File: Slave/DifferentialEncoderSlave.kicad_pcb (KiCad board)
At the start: 4 copper layers, 20 x 29 mm, 17 parts, among them J1 RJ45_Shielded, U1 SN75C1167, U2 MA730, U3 LDFM33PVR

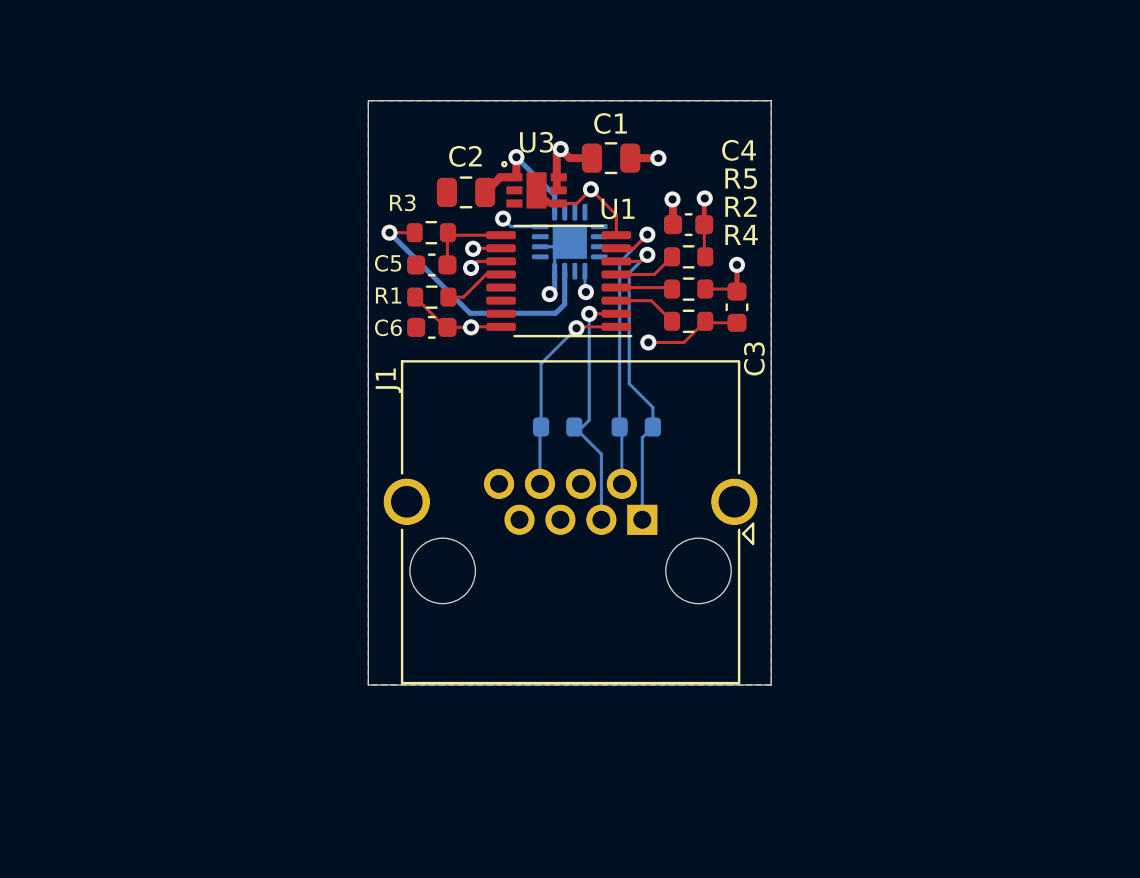
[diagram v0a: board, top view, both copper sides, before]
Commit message: Update board outline
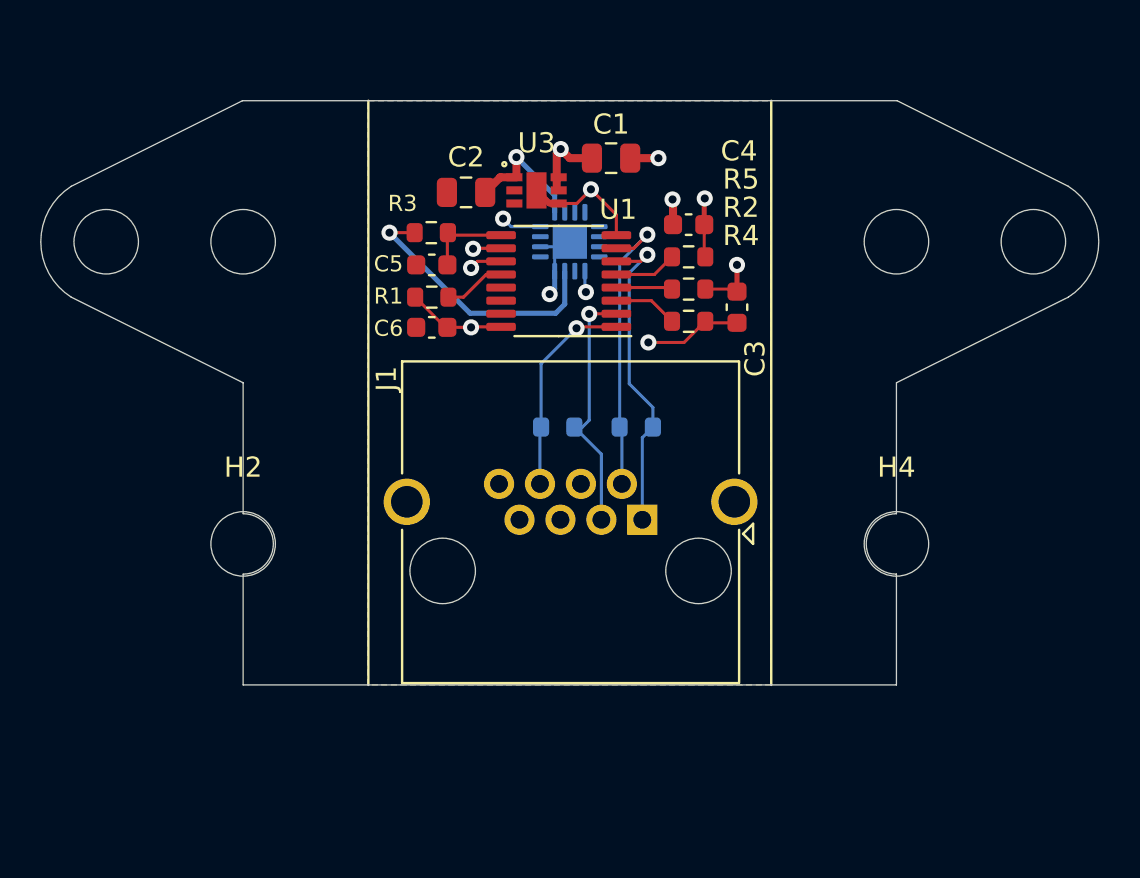
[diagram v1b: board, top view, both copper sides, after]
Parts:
- added H1: MountingHole, MountingHole:MountingHole_3.2mm_M3_DIN965, F.Cu at (138.2, 68.0)
- added H2: MountingHole, MountingHole:MountingHole_3.2mm_M3_DIN965, F.Cu at (105.8, 83.0)
- added H3: MountingHole, MountingHole:MountingHole_3.2mm_M3_DIN965, F.Cu at (105.8, 68.0)
- added H4: MountingHole, MountingHole:MountingHole_3.2mm_M3_DIN965, F.Cu at (138.2, 83.0)
- added H5: MountingHole, MountingHole:MountingHole_3.2mm_M3_DIN965, F.Cu at (99.0, 68.0)
- added H6: MountingHole, MountingHole:MountingHole_3.2mm_M3_DIN965, F.Cu at (145.0, 68.0)
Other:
- board size 20 x 29 mm -> 52.5 x 29 mm

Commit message: Use 3mm holes
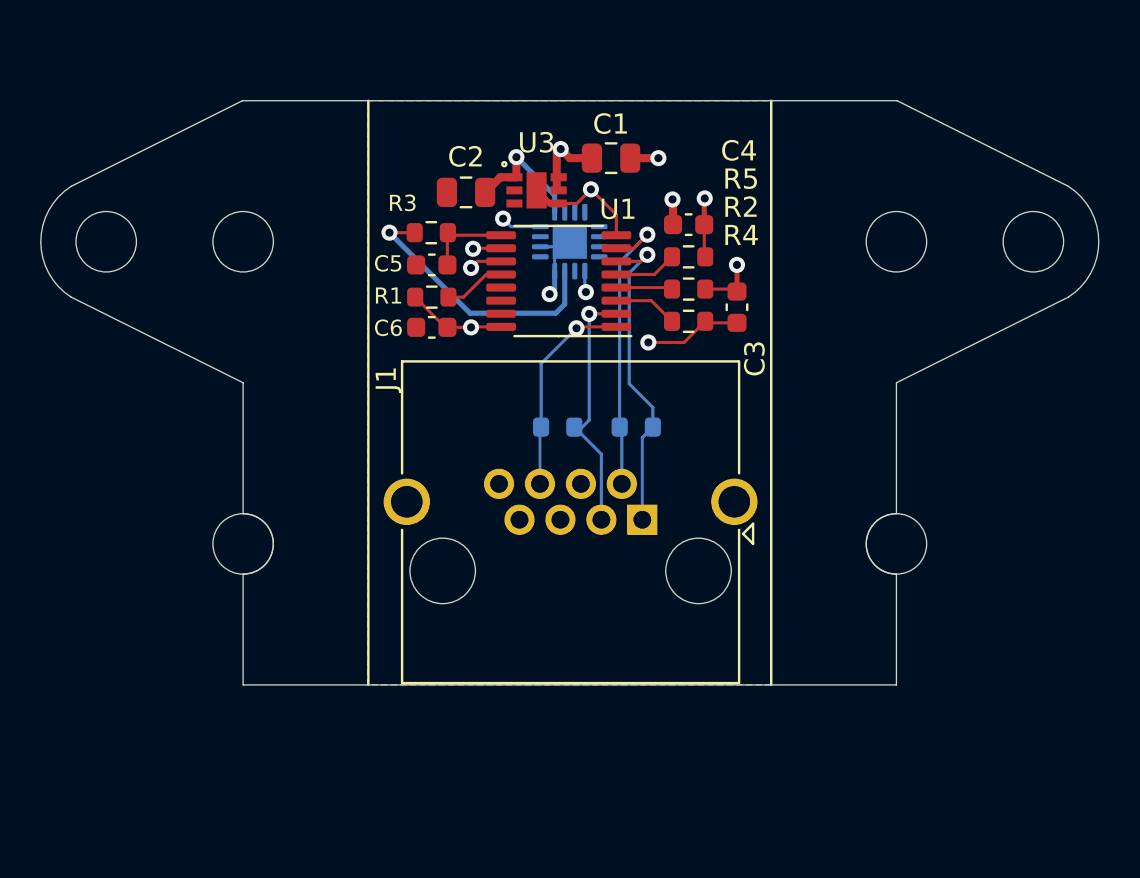
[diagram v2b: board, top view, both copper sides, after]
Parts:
- H1, H2, H3, H4, H5, H6: footprint MountingHole:MountingHole_3.2mm_M3_DIN965 -> MountingHole:MountingHole_3mm
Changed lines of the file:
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@@
     (add_net "Net-(U3-Pad3)")
   )
-  (module MountingHole:MountingHole_3.2mm_M3_DIN965 (layer F.Cu)
+  (module MountingHole:MountingHole_3mm (layer F.Cu)
     (at 138.215 83)
-    (descr "Mounting Hole 3.2mm, no annular, M3, DIN965")
-    (tags "mounting hole 3.2mm no annular m3 din965")
+    (descr "Mounting Hole 3mm, no annular")
+    (tags "mounting hole 3mm no annular")
     (attr virtual)
-    (fp_text reference H4 (at 0 -3.8) (layer F.SilkS)
+    (fp_text reference H4 (at -2.215 -4) (layer F.SilkS) hide
       (effects (font (size 1 1) (thickness 0.15)))
     )
-    (fp_text value MountingHole (at 0 3.8) (layer F.Fab)
+    (fp_text value MountingHole (at 0 4) (layer F.Fab)
       (effects (font (size 1 1) (thickness 0.15)))
     )
@@
       (effects (font (size 1 1) (thickness 0.15)))
     )
-    (fp_circle (center 0 0) (end 2.8 0) (layer Cmts.User) (width 0.15))
-    (fp_circle (center 0 0) (end 3.05 0) (layer F.CrtYd) (width 0.05))
-    (pad 1 np_thru_hole circle (at 0 0) (size 3.2 3.2) (drill 3.2) (layers *.Cu *.Mask))
+    (fp_circle (center 0 0) (end 3 0) (layer Cmts.User) (width 0.15))
+    (fp_circle (center 0 0) (end 3.25 0) (layer F.CrtYd) (width 0.05))
+    (pad 1 np_thru_hole circle (at 0 0) (size 3 3) (drill 3) (layers *.Cu *.Mask))
   )
-  (module MountingHole:MountingHole_3.2mm_M3_DIN965 (layer F.Cu)
+  (module MountingHole:MountingHole_3mm (layer F.Cu)
     (at 105.785 83)
-    (descr "Mounting Hole 3.2mm, no annular, M3, DIN965")
-    (tags "mounting hole 3.2mm no annular m3 din965")
+    (descr "Mounting Hole 3mm, no annular")
+    (tags "mounting hole 3mm no annular")
     (attr virtual)
-    (fp_text reference H2 (at 0 -3.8) (layer F.SilkS)
+    (fp_text reference H2 (at 2.215 -3.75) (layer F.SilkS) hide
       (effects (font (size 1 1) (thickness 0.15)))
     )
-    (fp_text value MountingHole (at 0 3.8) (layer F.Fab)
+    (fp_text value MountingHole (at 0 4) (layer F.Fab)
       (effects (font (size 1 1) (thickness 0.15)))
     )
@@
       (effects (font (size 1 1) (thickness 0.15)))
     )
-    (fp_circle (center 0 0) (end 2.8 0) (layer Cmts.User) (width 0.15))
-    (fp_circle (center 0 0) (end 3.05 0) (layer F.CrtYd) (width 0.05))
-    (pad 1 np_thru_hole circle (at 0 0) (size 3.2 3.2) (drill 3.2) (layers *.Cu *.Mask))
+    (fp_circle (center 0 0) (end 3 0) (layer Cmts.User) (width 0.15))
+    (fp_circle (center 0 0) (end 3.25 0) (layer F.CrtYd) (width 0.05))
+    (pad 1 np_thru_hole circle (at 0 0) (size 3 3) (drill 3) (layers *.Cu *.Mask))
   )
-  (module MountingHole:MountingHole_3.2mm_M3_DIN965 (layer F.Cu)
+  (module MountingHole:MountingHole_3mm (layer F.Cu)
     (at 145.0125 68)
-    (descr "Mounting Hole 3.2mm, no annular, M3, DIN965")
-    (tags "mounting hole 3.2mm no annular m3 din965")
+    (descr "Mounting Hole 3mm, no annular")
+    (tags "mounting hole 3mm no annular")
     (attr virtual)
-    (fp_text reference H6 (at 0 -3.8) (layer F.SilkS) hide
+    (fp_text reference H6 (at -3.0125 -3.5) (layer F.SilkS) hide
       (effects (font (size 1 1) (thickness 0.15)))
     )
-    (fp_text value MountingHole (at 0 3.8) (layer F.Fab)
+    (fp_text value MountingHole (at 0 4) (layer F.Fab)
       (effects (font (size 1 1) (thickness 0.15)))
     )
@@
       (effects (font (size 1 1) (thickness 0.15)))
     )
-    (fp_circle (center 0 0) (end 2.8 0) (layer Cmts.User) (width 0.15))
-    (fp_circle (center 0 0) (end 3.05 0) (layer F.CrtYd) (width 0.05))
-    (pad 1 np_thru_hole circle (at 0 0) (size 3.2 3.2) (drill 3.2) (layers *.Cu *.Mask))
+    (fp_circle (center 0 0) (end 3 0) (layer Cmts.User) (width 0.15))
+    (fp_circle (center 0 0) (end 3.25 0) (layer F.CrtYd) (width 0.05))
+    (pad 1 np_thru_hole circle (at 0 0) (size 3 3) (drill 3) (layers *.Cu *.Mask))
   )
-  (module MountingHole:MountingHole_3.2mm_M3_DIN965 (layer F.Cu)
+  (module MountingHole:MountingHole_3mm (layer F.Cu)
     (at 98.9875 68)
-    (descr "Mounting Hole 3.2mm, no annular, M3, DIN965")
-    (tags "mounting hole 3.2mm no annular m3 din965")
+    (descr "Mounting Hole 3mm, no annular")
+    (tags "mounting hole 3mm no annular")
     (attr virtual)
-    (fp_text reference H5 (at 0 -3.8) (layer F.SilkS) hide
+    (fp_text reference H5 (at 3.5125 -3.5) (layer F.SilkS) hide
       (effects (font (size 1 1) (thickness 0.15)))
     )
-    (fp_text value MountingHole (at 0 3.8) (layer F.Fab)
+    (fp_text value MountingHole (at 0 4) (layer F.Fab)
       (effects (font (size 1 1) (thickness 0.15)))
     )
@@
       (effects (font (size 1 1) (thickness 0.15)))
     )
-    (fp_circle (center 0 0) (end 2.8 0) (layer Cmts.User) (width 0.15))
-    (fp_circle (center 0 0) (end 3.05 0) (layer F.CrtYd) (width 0.05))
-    (pad 1 np_thru_hole circle (at 0 0) (size 3.2 3.2) (drill 3.2) (layers *.Cu *.Mask))
+    (fp_circle (center 0 0) (end 3 0) (layer Cmts.User) (width 0.15))
+    (fp_circle (center 0 0) (end 3.25 0) (layer F.CrtYd) (width 0.05))
+    (pad 1 np_thru_hole circle (at 0 0) (size 3 3) (drill 3) (layers *.Cu *.Mask))
   )
-  (module MountingHole:MountingHole_3.2mm_M3_DIN965 (layer F.Cu)
-    (at 138.215 68)
-    (descr "Mounting Hole 3.2mm, no annular, M3, DIN965")
-    (tags "mounting hole 3.2mm no annular m3 din965")
+  (module MountingHole:MountingHole_3mm (layer F.Cu)
+    (at 105.785 68)
+    (descr "Mounting Hole 3mm, no annular")
+    (tags "mounting hole 3mm no annular")
     (attr virtual)
-    (fp_text reference H1 (at -3.965 -3.25) (layer F.SilkS) hide
+    (fp_text reference H3 (at 0 -4) (layer F.SilkS) hide
       (effects (font (size 1 1) (thickness 0.15)))
     )
-    (fp_text value MountingHole (at 0 3.8) (layer F.Fab)
+    (fp_text value MountingHole (at 0 4) (layer F.Fab)
       (effects (font (size 1 1) (thickness 0.15)))
     )
@@
       (effects (font (size 1 1) (thickness 0.15)))
     )
-    (fp_circle (center 0 0) (end 2.8 0) (layer Cmts.User) (width 0.15))
-    (fp_circle (center 0 0) (end 3.05 0) (layer F.CrtYd) (width 0.05))
-    (pad 1 np_thru_hole circle (at 0 0) (size 3.2 3.2) (drill 3.2) (layers *.Cu *.Mask))
+    (fp_circle (center 0 0) (end 3 0) (layer Cmts.User) (width 0.15))
+    (fp_circle (center 0 0) (end 3.25 0) (layer F.CrtYd) (width 0.05))
+    (pad 1 np_thru_hole circle (at 0 0) (size 3 3) (drill 3) (layers *.Cu *.Mask))
   )
-  (module MountingHole:MountingHole_3.2mm_M3_DIN965 (layer F.Cu)
-    (at 105.785 68)
-    (descr "Mounting Hole 3.2mm, no annular, M3, DIN965")
-    (tags "mounting hole 3.2mm no annular m3 din965")
+  (module MountingHole:MountingHole_3mm (layer F.Cu)
+    (at 138.215 68)
+    (descr "Mounting Hole 3mm, no annular")
+    (tags "mounting hole 3mm no annular")
     (attr virtual)
-    (fp_text reference H3 (at 2.465 -3.25) (layer F.SilkS) hide
+    (fp_text reference H1 (at 0 -4) (layer F.SilkS) hide
       (effects (font (size 1 1) (thickness 0.15)))
     )
-    (fp_text value MountingHole (at 0 3.8) (layer F.Fab)
+    (fp_text value MountingHole (at 0 4) (layer F.Fab)
       (effects (font (size 1 1) (thickness 0.15)))
     )
@@
       (effects (font (size 1 1) (thickness 0.15)))
     )
-    (fp_circle (center 0 0) (end 2.8 0) (layer Cmts.User) (width 0.15))
-    (fp_circle (center 0 0) (end 3.05 0) (layer F.CrtYd) (width 0.05))
-    (pad 1 np_thru_hole circle (at 0 0) (size 3.2 3.2) (drill 3.2) (layers *.Cu *.Mask))
+    (fp_circle (center 0 0) (end 3 0) (layer Cmts.User) (width 0.15))
+    (fp_circle (center 0 0) (end 3.25 0) (layer F.CrtYd) (width 0.05))
+    (pad 1 np_thru_hole circle (at 0 0) (size 3 3) (drill 3) (layers *.Cu *.Mask))
   )
   (module Wetmelon:DFN6-2x2 (layer F.Cu)

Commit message: Update Slave with circular keepout, SMD RJ 45
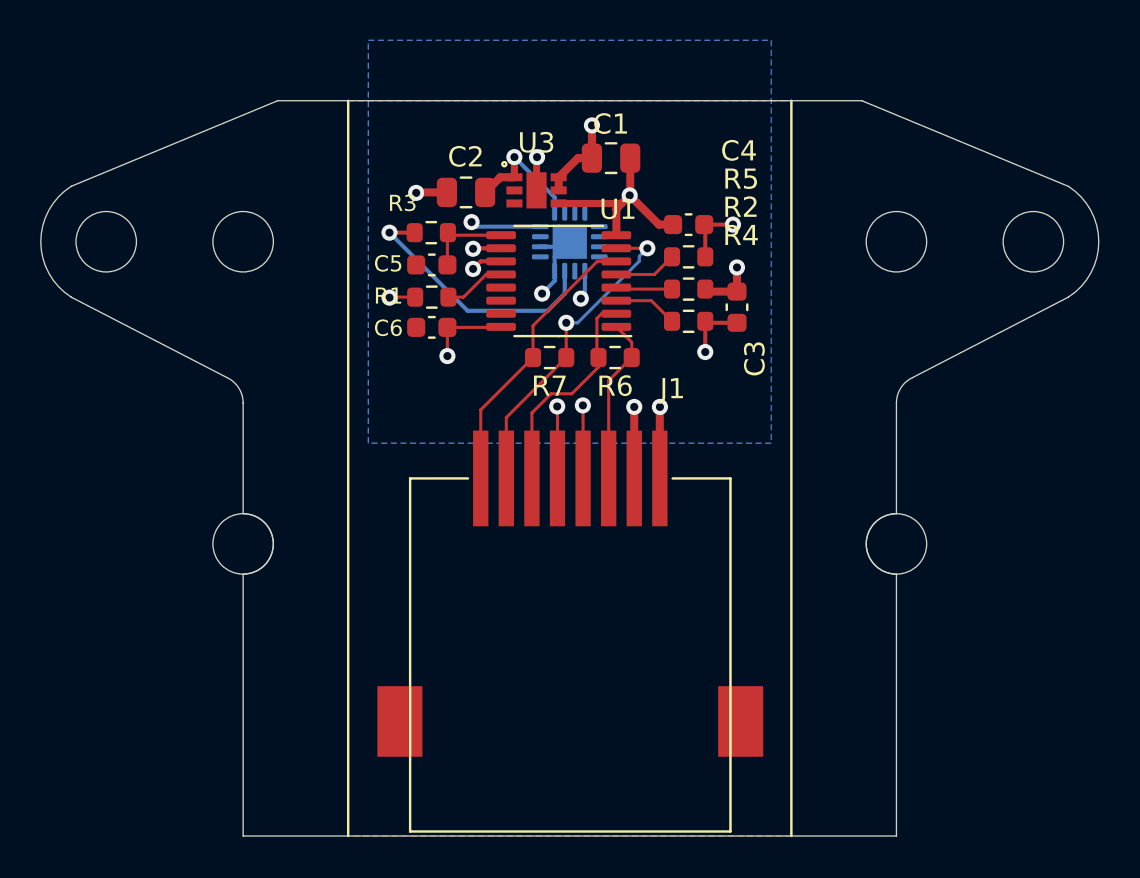
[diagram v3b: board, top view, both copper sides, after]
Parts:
- J1: footprint Connector_RJ:RJ45_Amphenol_RJHSE5380 -> Wetmelon:RJLSE4118101
- R6, R7: moved to F.Cu
- moved R7 5.51 mm to (121.0, 73.8), turned to 180 degrees
- moved R6 4.47 mm to (124.2, 73.8), turned to 180 degrees
- moved J1 4.12 mm to (122.0, 79.8), turned to 0 degrees
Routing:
- net GNDD: track 16.1 -> 24.8 mm, vias 5 -> 6
- net +5V: track 8.76 -> 13.3 mm, vias 2 -> 4
- net /CLK: track 19.0 -> 22.2 mm
- net /MISO+: track 18.1 -> 15.1 mm, vias 1 -> 2
- net /CLK-: track 10.5 -> 8.32 mm, vias 1 -> 0
- net /CSn+: track 15.9 -> 14.1 mm, vias 1 -> 0
- net /CLK+: track 12.7 -> 11.0 mm, vias 1 -> 0
- net /CSn-: track 14.8 -> 16.2 mm, vias 1 -> 2
- net /MISO-: track 14.6 -> 13.7 mm, vias 1 -> 2
- net /CSn: track 13.0 -> 13.6 mm
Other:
- board size 52.5 x 29 mm -> 52.5 x 36.5 mm
- board text added: "Keepout"

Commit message: Make the body narrower
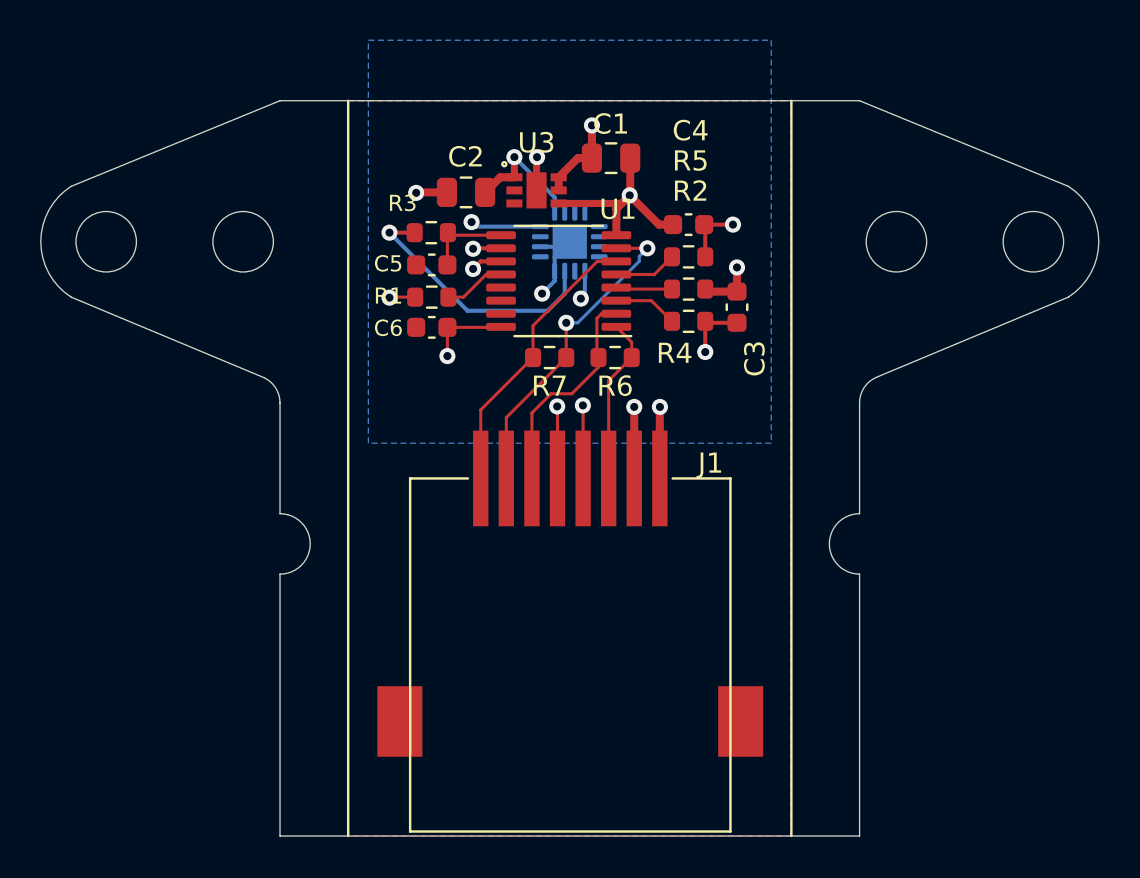
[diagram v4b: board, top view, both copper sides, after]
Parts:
- removed H2, H4: MountingHole, MountingHole:MountingHole_3mm
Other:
- outline, holes or cut-outs redrawn
